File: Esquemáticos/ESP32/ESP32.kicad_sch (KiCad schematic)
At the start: 0 parts

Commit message: añadí leds
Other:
- note added: "Rta/ yo no lo ocupo, no sé si alguien si -Raúl"
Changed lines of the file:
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@@
+    (effects (font (size 1.27 1.27)) (justify left bottom))
+  )
+  (text "Rta/ yo no lo ocupo, no sé si alguien si\n-Raúl\n" (at 156.21 109.22 0)
     (effects (font (size 1.27 1.27)) (justify left bottom))
   )
@@
     )
     (path "/befd95e3-f29f-4265-b7f4-12932b391cda/e30690a4-66e5-4d57-a707-b43d3ee6e681"
-      (reference "R28") (unit 1) (value "10k") (footprint "Resistor_SMD:R_1206_3216Metric_Pad1.30x1.75mm_HandSolder")
+      (reference "R28") (unit 1) (value "56") (footprint "Resistor_SMD:R_1206_3216Metric_Pad1.30x1.75mm_HandSolder")
+    )
+    (path "/3dc66758-7067-4285-a03f-e9474bf12d83/dcf91bd7-bd3a-4623-adf2-7cfee1fb67ef"
+      (reference "R29") (unit 1) (value "56") (footprint "Resistor_SMD:R_1206_3216Metric_Pad1.30x1.75mm_HandSolder")
     )
     (path "/befd95e3-f29f-4265-b7f4-12932b391cda/4989dbdc-323d-4a36-967e-1585d6ae2f13"

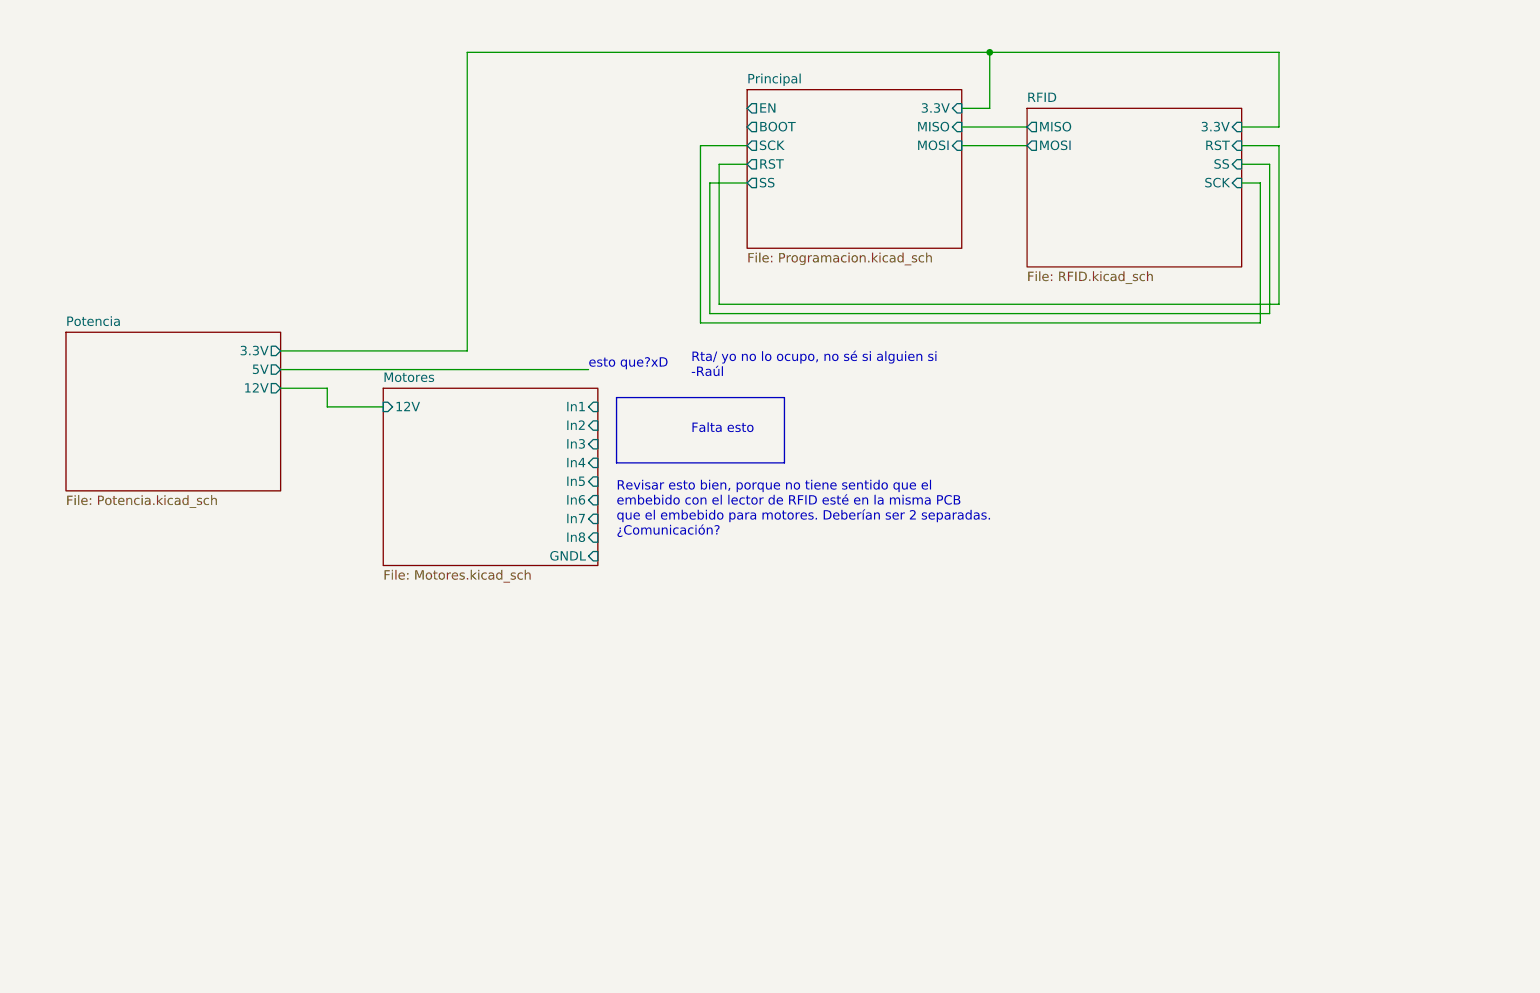
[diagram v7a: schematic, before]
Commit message: Muchos cambios a la PCB
Moví varios elementos para poder añadir los agujeros de montaje y agregué esos agujeros de montaje.

También moví el pulsador de BOOT para que quede estéticamente mejor a ambos lados del módulo ESP32 WROOM

Importante:
Nos faltan todas las conexiones de los optoacopladores con la ESP 32 xD (urgente revisar cuales pines sirven para eso).
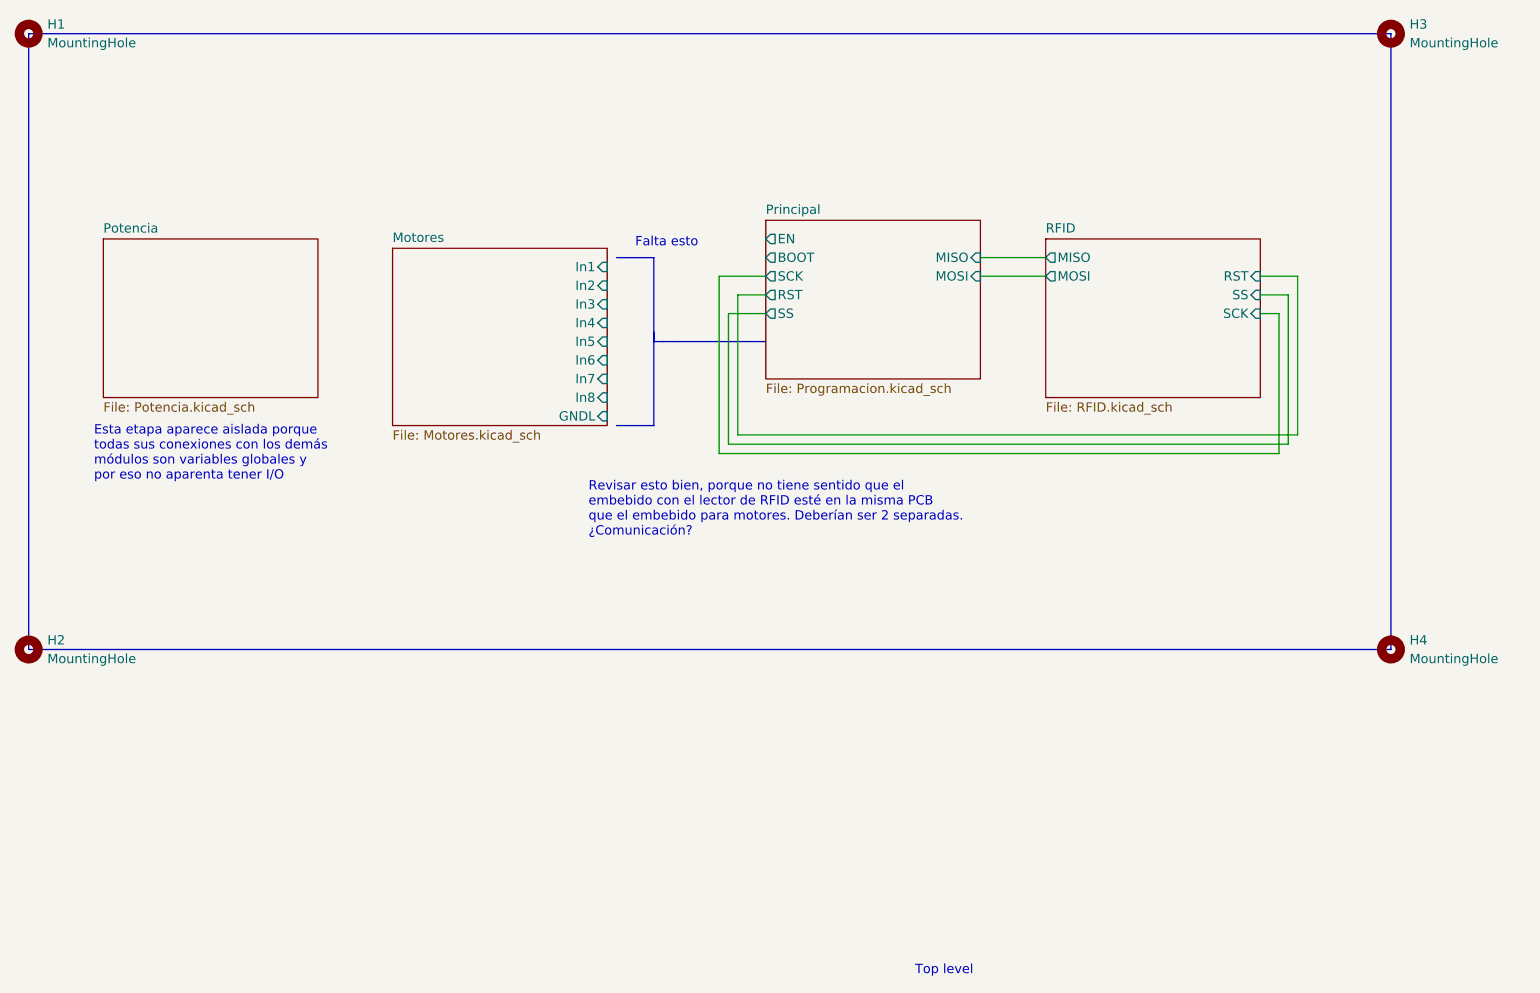
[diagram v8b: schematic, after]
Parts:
- added H1, H2, H3, H4: MountingHole, MountingHole:MountingHole_2.5mm, symbol Mechanical:MountingHole
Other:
- sheet Motores ports: added none; removed 12V
- sheet Potencia ports: added none; removed 12V, 3.3V, 5V
- sheet Principal ports: added none; removed 3.3V
- sheet RFID ports: added none; removed 3.3V
- note added: "Esta etapa aparece aislada porque todas sus conexiones con los demás módulos son variables globales y por eso no aparenta tener I/O"
- note added: "Top level"
- note removed: "Rta/ yo no lo ocupo, no sé si alguien si -Raúl"
- note removed: "esto que?xD"
